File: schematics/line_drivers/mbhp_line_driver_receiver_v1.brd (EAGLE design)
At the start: 56.6 x 53.3 mm, 23 parts, among them IC1 MC3486, IC2 MC3486

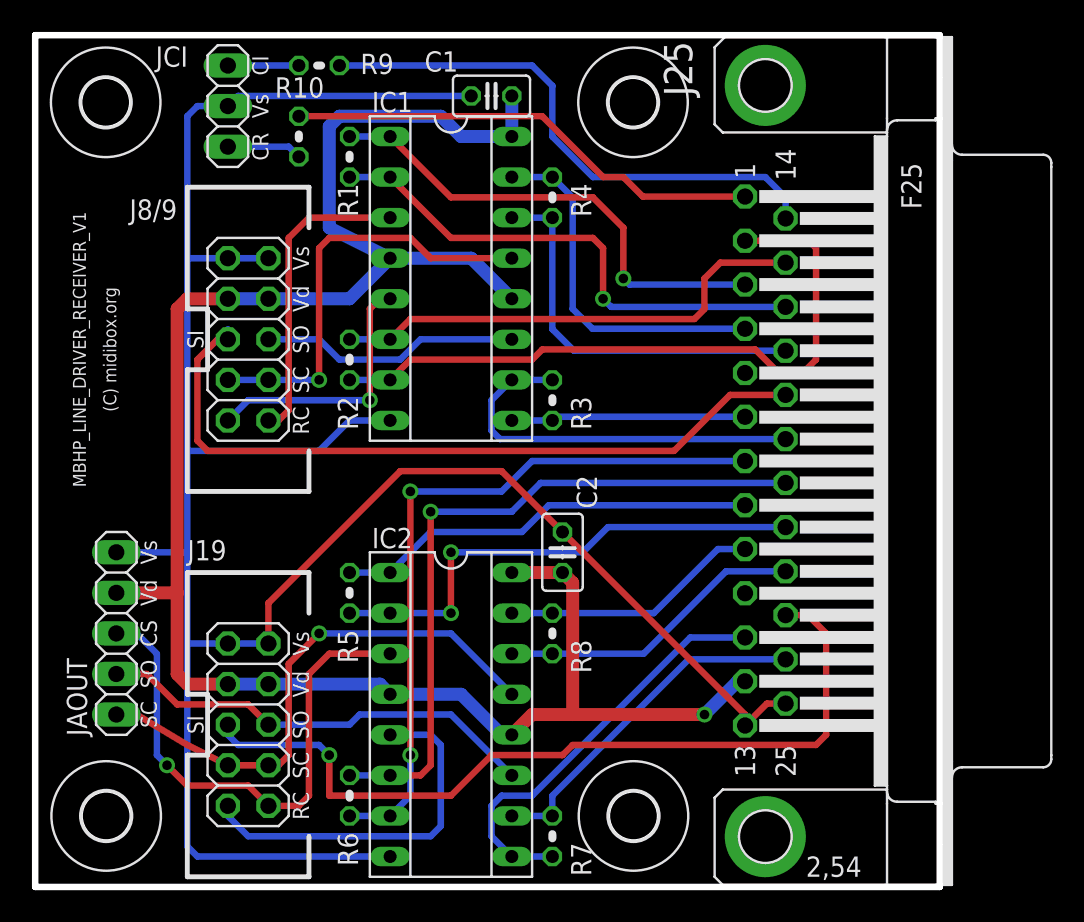
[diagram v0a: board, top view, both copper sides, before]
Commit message: mbhp_line_driver: make PCBs smaller
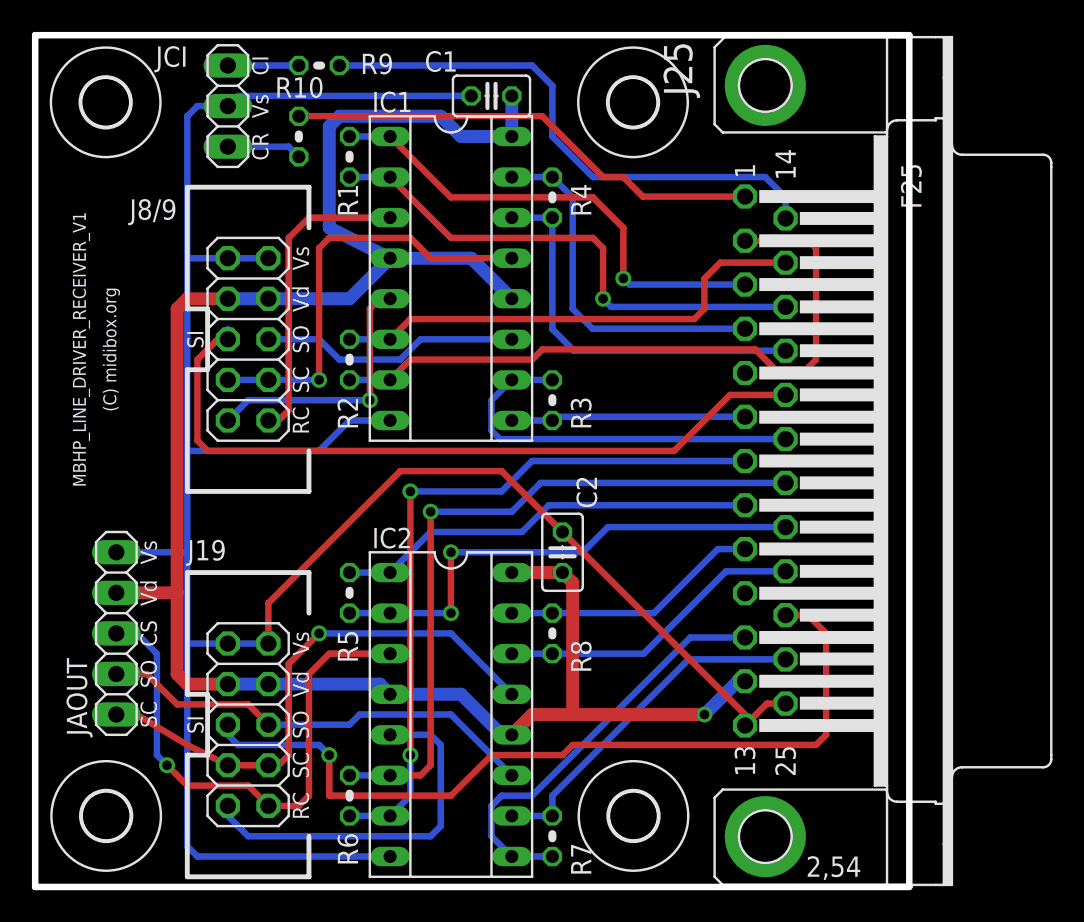
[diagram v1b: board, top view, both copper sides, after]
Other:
- board size 56.6 x 53.3 mm -> 54.7 x 53.3 mm
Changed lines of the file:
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@@
 <plain>
 <wire x1="0" y1="0" x2="0" y2="53.335" width="0.4064" layer="20"/>
-<wire x1="0" y1="53.335" x2="56.64" y2="53.335" width="0.4064" layer="20"/>
-<wire x1="56.64" y1="53.335" x2="56.64" y2="0" width="0.4064" layer="20"/>
-<wire x1="56.64" y1="0" x2="0" y2="0" width="0.4064" layer="20"/>
+<wire x1="0" y1="53.335" x2="54.735" y2="53.335" width="0.4064" layer="20"/>
+<wire x1="54.735" y1="53.335" x2="54.735" y2="0" width="0.4064" layer="20"/>
+<wire x1="54.735" y1="0" x2="0" y2="0" width="0.4064" layer="20"/>
 <wire x1="9.525" y1="19.685" x2="17.145" y2="19.685" width="0.3048" layer="25"/>
 <wire x1="17.145" y1="19.685" x2="17.145" y2="17.145" width="0.3048" layer="25"/>
@@
 <polygon width="0.4064" layer="1">
 <vertex x="0" y="53.34"/>
-<vertex x="56.515" y="53.34"/>
-<vertex x="56.515" y="0"/>
+<vertex x="54.61" y="53.34"/>
+<vertex x="54.61" y="0"/>
 <vertex x="0" y="0"/>
 </polygon>
 <polygon width="0.4064" layer="16">
 <vertex x="0" y="53.34"/>
-<vertex x="56.515" y="53.34"/>
-<vertex x="56.515" y="0"/>
+<vertex x="54.61" y="53.34"/>
+<vertex x="54.61" y="0"/>
 <vertex x="0" y="0"/>
 </polygon>
